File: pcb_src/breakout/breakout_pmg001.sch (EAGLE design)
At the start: 26 parts

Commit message: Reworked repository
Name changed, added a lot of new resources etc.
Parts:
- removed C3, C4, C5, C6: 100nF, eagle-ltspice:CC0603
- removed LED1: (no value), led:LEDCHIPLED_1206
- removed R11, R12, R7: 5.1k, rcl:R-EU_R0603
- removed R8: 470R, rcl:R-EU_R0603
- removed SPEAKER_CON1: JST_HEADER_2MM_2P, edrtech_lib:JST_HEADER_2MM_2P
- removed U$3: TS-1101VS-C-A-A, circuitmess_device_library:TS-1101VS-C-A-A
- removed U$5: CH340C, circuitmess_device_library:CH340C
- removed U$6: USB-C, edrtech_lib:USB-C
- added C1: 1u, rcl:C-EUC0402
- added C2: 10n, rcl:C-EUC0402
- added C7, C8, C9: 100nF, rcl:C-EUC0402
- added IC1: SN74AUP2G00DCUR, SN74AUP2G00DCUR:SN74AUP2G00DCUR
- added LED2, LED4, LED5: (no value), led:LEDCHIP-LED0603
- added R1: 100k, rcl:R-EU_R0402
- added R2: 10k, rcl:R-EU_R0402
- added R3, R4: 5.1k, rcl:R-EU_R0402
- added R9: 470R, rcl:R-EU_R0402
- added S5: TS3A5223RSWR, TS3A5223RSWR:TS3A5223RSWR
- added TP1, TP2: TPSQTP19SQ, testpad:TPSQTP19SQ
- added U$12: USB-C, edrtech_lib:USB-C
- added U2: CH340E_MSOP10, CH340E:CH340E_MSOP10
- D1: value BAT54 -> BAT54WS-13P; device diode:BAT54 -> BAT54WS-13P:BAT54WS-13P
- R5, R6: device rcl:R-EU_R0603 -> rcl:R-EU_R0402
- U$1: value CH340C -> TS-1101S; device circuitmess_device_library:CH340C -> edrtech_lib:TS-1101S
- U$4: value USB-C -> TS-1101S; device edrtech_lib:USB-C -> edrtech_lib:TS-1101S
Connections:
- removed net D+_AT: U$1.UD+, U$4.DP1, U$4.DP2
- removed net D+_U: U$5.UD+, U$6.DP1, U$6.DP2
- removed net D-_AT: U$1.UD-, U$4.DN1, U$4.DN2
- removed net D-_U: U$5.UD-, U$6.DN1, U$6.DN2
- removed net N$5: R7.1, U$6.CC2
- removed net N$8: R11.2, U$4.CC1
- removed net N$9: R12.1, U$4.CC2
- new net D+: U$12.DP1, U$12.DP2, U2.UD+
- new net D-: U$12.DN1, U$12.DN2, U2.UD-
- new net N$1: C2.2, IC1.1A, IC1.1B, R2.1, U$2.P$2
- new net N$11: C1.1, R1.1, U$2.P$1
- new net N$2: R3.2, U$12.CC1
- new net N$6: R4.1, U$12.CC2
- new net N$7: IC1.1Y, IC1.2A, IC1.2B, R1.2
- new net RXI: S5.COM2, U2.RXI
- new net SEL: IC1.2Y, R2.2, R6.2, S5.SEL1, S5.SEL2
- new net TXO: S5.COM1, U2.TXO
- net 3V3: now also C7.2, C8.2, C9.1, IC1.VCC, S5.VCC, U2.V3, U2.VCC; no longer C3.2, C4.2, C5.2, C6.2, U$1.V3, U$1.VCC, U$5.V3, U$5.VCC
- net 5V: now also U$12.VCC; no longer U$4.VCC, U$6.VCC
- net AT_RXD: now also S5.NO1; no longer U$1.TXD
- net AT_TXD: now also S5.NO2; no longer U$1.RXD
- net BAT: now also TP1.TP; no longer SPEAKER_CON1.+
- net GND: now also C1.2, C2.1, C7.1, C8.1, C9.2, IC1.GND, LED2.C, LED4.A, LED5.C, R3.1, R4.2, S5.GND, TP2.TP, U$1.1, U$12.GND, U$4.1, U2.GND; no longer C3.1, C4.1, C5.1, C6.1, LED1.C, R11.1, R12.2, R6.1, R7.2, SPEAKER_CON1.-, U$1.GND, U$2.P$1, U$3.P$2, U$4.GND, U$5.GND, U$6.GND
- net N$3: now also LED2.A; no longer LED1.A
- net N$4: now also LED4.C, LED5.A, R6.1; no longer R6.2, U$6.CC1
- net PA3: now also U$1.2; no longer U$2.P$2
- net PWR_SW: now also U$4.2; no longer U$3.P$1
- net UPDI: now also R9.1; no longer R8.1
- net UPDI_RX: now also R9.2, S5.NC2; no longer R8.2, U$5.RXD
- net UPDI_TX: now also D1.K, S5.NC1; no longer D1.C, U$5.TXD
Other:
- note added: "13.10.2024."
- note added: "PMG001/bATtiny Guard BREAKOUT BOARD"
- note removed: "10.07.2024."
- note removed: "PMG001 BREAKOUT BOARD"
- moved on the sheet: D1, JP1, JP2, R6

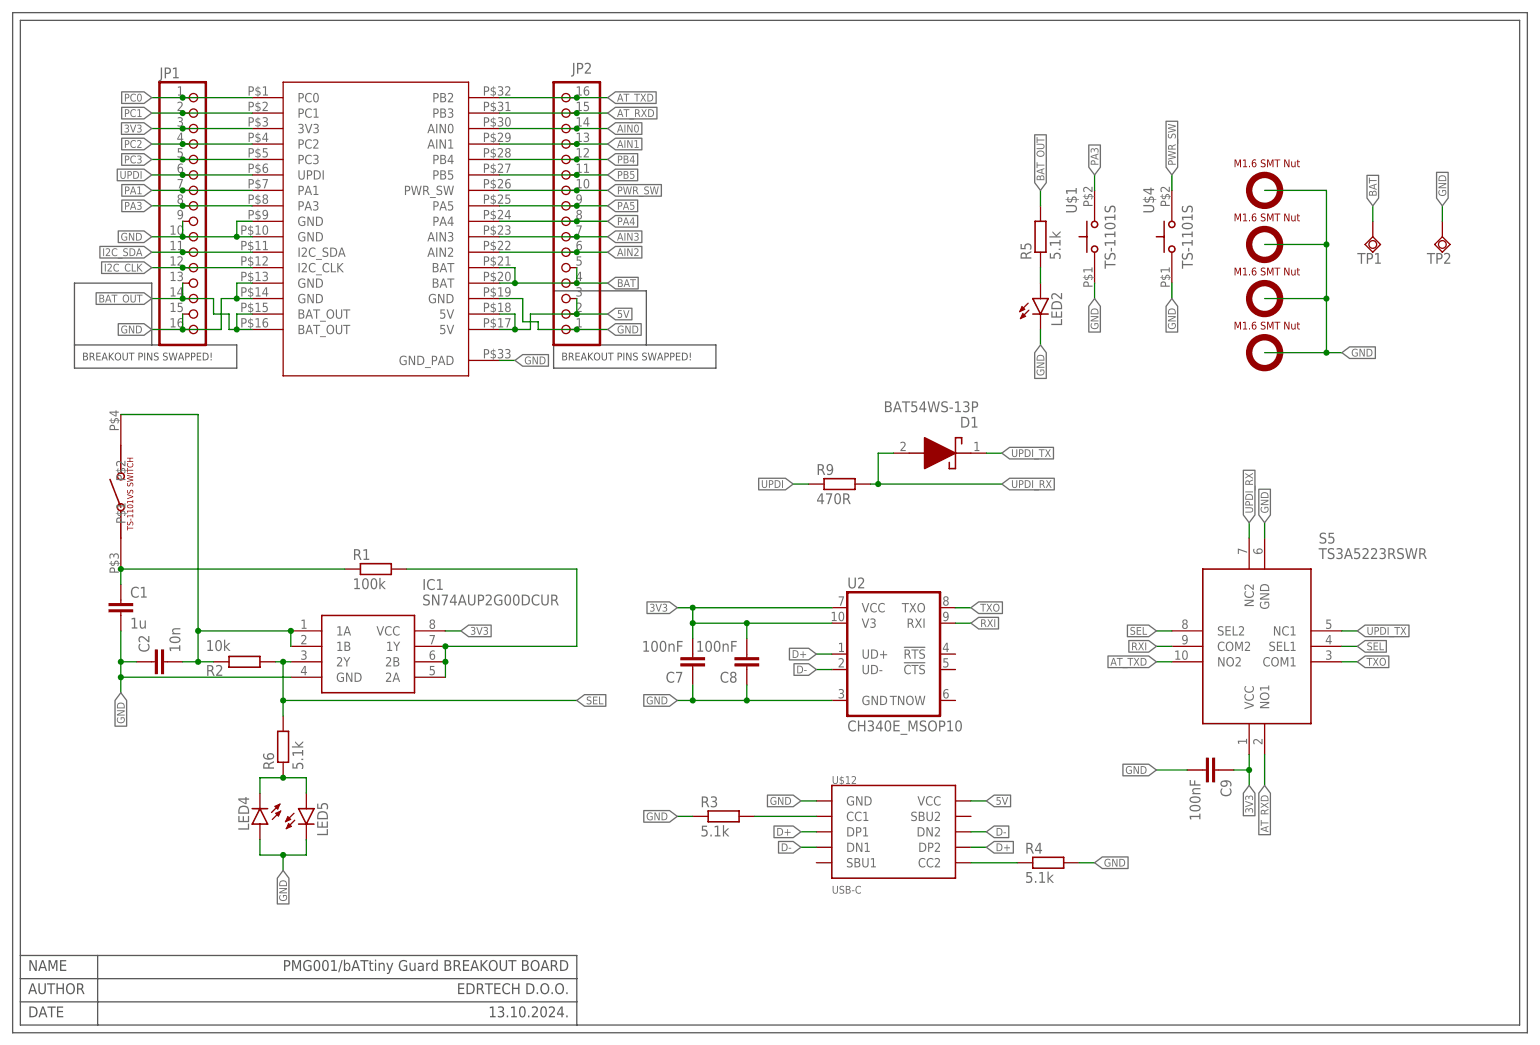
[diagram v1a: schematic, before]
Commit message: Updated to latest revision
Documentation updated to match the latest hardware revision.
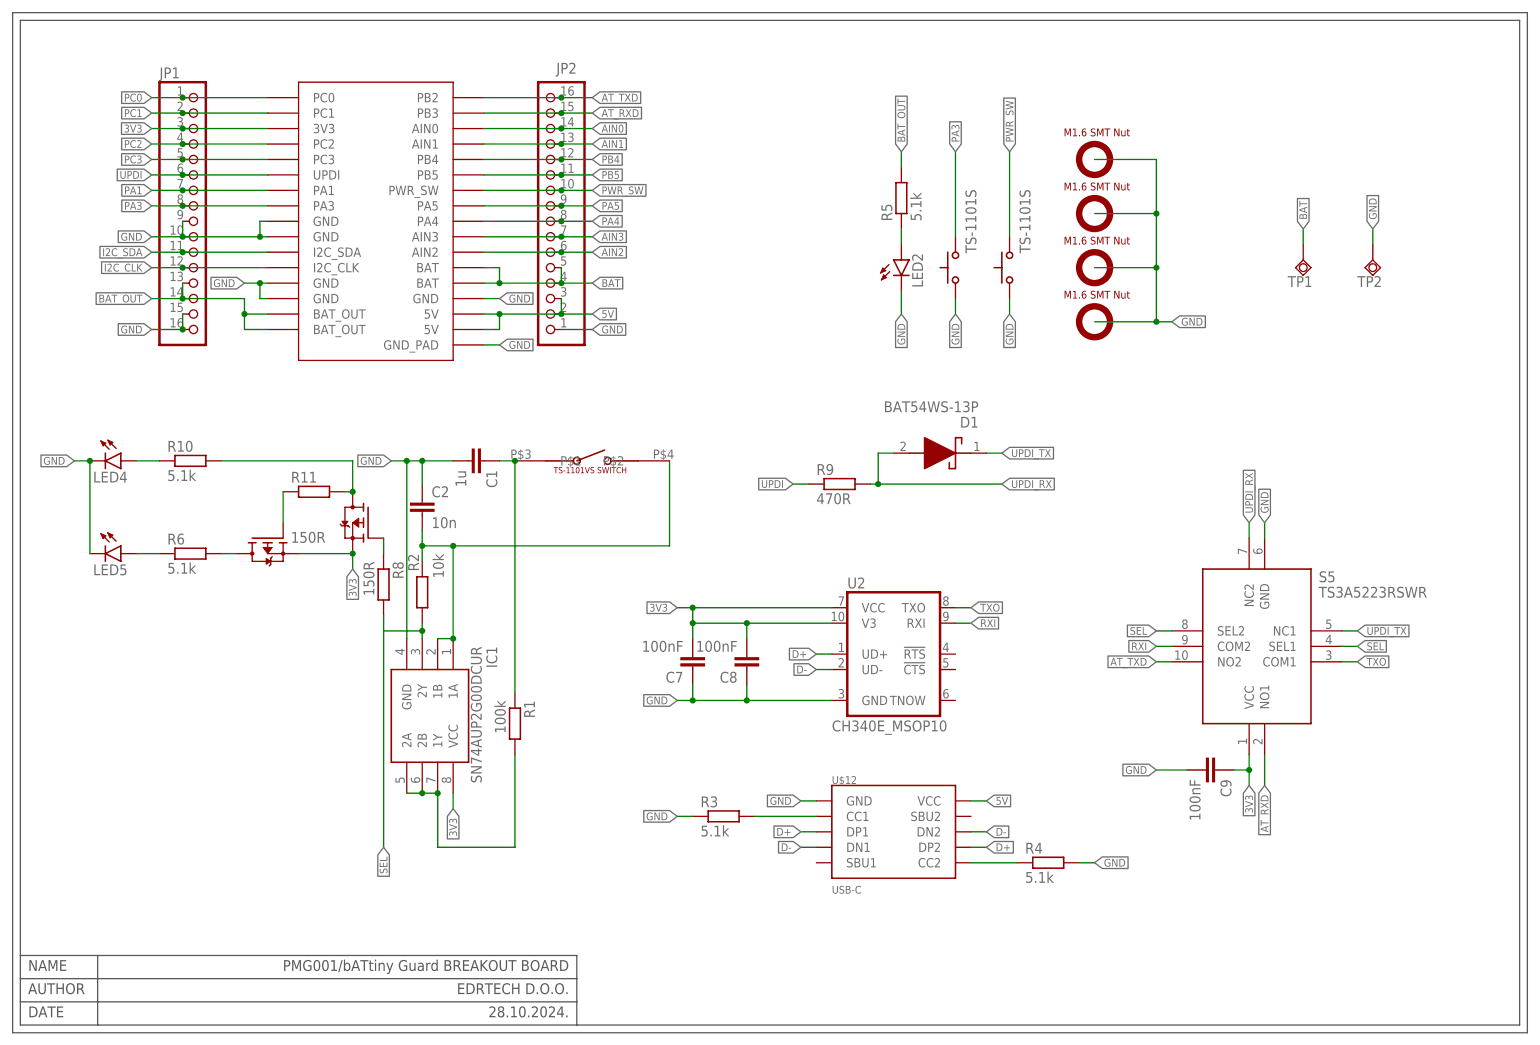
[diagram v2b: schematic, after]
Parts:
- added Q1, Q2: NTK3139PT1G, edrtech_lib:NTK3139PT1G
- added R10: 5.1k, rcl:R-EU_R0402
- added R11, R8: 150R, rcl:R-EU_R0402
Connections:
- new net N$10: LED4.A, R10.1
- new net N$12: Q2.G, R11.1
- new net N$5: Q1.G, R8.1
- new net N$8: Q1.D, R10.2, R11.2
- new net N$9: Q2.D, R6.2
- net 3V3: now also Q1.S, Q2.S
- net GND: now also LED4.C; no longer LED4.A
- net N$4: no longer LED4.C
- net SEL: now also R8.2; no longer R6.2
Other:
- note added: "28.10.2024."
- note removed: "13.10.2024."
- note removed: "BREAKOUT PINS SWAPPED!"
- moved on the sheet: C1, C2, IC1, JP2, LED2, LED4, LED5, R1, R2, R5, R6, TP1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
